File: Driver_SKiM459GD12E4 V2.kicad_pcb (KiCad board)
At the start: 4 copper layers, 169.2 x 116 mm, 97 parts, among them J13 EL1, J14 GL1, J15 NTC1_A, J16 NTC1_B, J17 GH1, J18 OUT1, J19 CH1, J20 EL2, J21 GL2, J22 NTC2_A, J23 NTC2_B, J24 GH2, J25 OUT2, J26 CH2, J27 EL3, J28 GL3, J29 NTC3_A, J30 NTC3_B, J31 GH3, J32 OUT3, J33 CH3

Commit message: Одна стойка
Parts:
- removed the C2 at (147.4, 114.2)
- removed the C2 at (196.2, 114.2)
- removed the C3 at (207.9, 92.6)
- removed the C3 at (159.1, 92.6)
- removed the C5 at (131.7, 114.4)
- removed the C5 at (180.5, 114.4)
- removed the C6 at (137.8, 92.6)
- removed the C6 at (186.6, 92.6)
- removed the D1 at (148.5, 105.8)
- removed the D1 at (197.2, 105.8)
- removed the D2 at (154.1, 74.3)
- removed the D2 at (202.8, 74.3)
- removed the D3 at (205.4, 92.1)
- removed the D3 at (156.6, 92.1)
- removed the D4 at (132.2, 105.8)
- removed the D4 at (181.0, 105.8)
- removed the D5 at (183.8, 92.1)
- removed the D5 at (135.0, 92.1)
- removed the D6 at (132.3, 74.3)
- removed the D6 at (181.1, 74.3)
- removed the R1 at (198.5, 114.2)
- removed the R1 at (149.7, 114.2)
- removed the R10 at (181.1, 92.6)
- removed the R10 at (132.3, 92.6)
- removed the R12 at (132.3, 82.9)
- removed the R12 at (181.1, 82.9)
- removed the R2 at (145.4, 90.6)
- removed the R2 at (194.2, 90.6)
- removed the R3 at (199.0, 90.6)
- removed the R3 at (150.2, 90.6)
- removed the R4 at (202.8, 82.9)
- removed the R4 at (154.1, 82.9)
- removed the R5 at (154.1, 92.6)
- removed the R5 at (202.8, 92.6)
- removed the R7 at (182.8, 114.4)
- removed the R7 at (134.0, 114.4)
- removed the R8 at (172.4, 90.8)
- removed the R8 at (123.7, 90.8)
- removed the R9 at (128.5, 90.8)
- removed the R9 at (177.3, 90.8)
- added C10: 2.2u, Capacitor_SMD:C_0805_2012Metric_Pad1.18x1.45mm_HandSolder, B.Cu at (97.8, 118.9)
- added C11: 56p, Capacitor_SMD:C_0805_2012Metric_Pad1.18x1.45mm_HandSolder, F.Cu at (74.2, 137.4)
- added C12: 56p, Capacitor_SMD:C_0805_2012Metric_Pad1.18x1.45mm_HandSolder, B.Cu at (67.3, 133.1)
- added C13: 56p, Capacitor_SMD:C_0805_2012Metric_Pad1.18x1.45mm_HandSolder, B.Cu at (90.2, 125.5)
- added C14: 56p, Capacitor_SMD:C_0805_2012Metric_Pad1.18x1.45mm_HandSolder, B.Cu at (86.6, 141.7)
- added C15: 56p, Capacitor_SMD:C_0805_2012Metric_Pad1.18x1.45mm_HandSolder, F.Cu at (92.7, 130.3)
- added C16: 56p, Capacitor_SMD:C_0805_2012Metric_Pad1.18x1.45mm_HandSolder, F.Cu at (92.7, 144.0)
- added C17: 56p, Capacitor_SMD:C_0805_2012Metric_Pad1.18x1.45mm_HandSolder, F.Cu at (92.7, 134.9)
- added C18: 56p, Capacitor_SMD:C_0805_2012Metric_Pad1.18x1.45mm_HandSolder, F.Cu at (92.7, 139.4)
- added C19: 10u, Capacitor_SMD:C_1210_3225Metric_Pad1.33x2.70mm_HandSolder, F.Cu at (82.3, 118.9)
- added C20: 10u, Capacitor_SMD:C_1210_3225Metric_Pad1.33x2.70mm_HandSolder, F.Cu at (93.0, 118.9)
- added C21: 1u, Capacitor_SMD:C_0805_2012Metric_Pad1.18x1.45mm_HandSolder, B.Cu at (102.6, 99.6)
- added C22: 1u, Capacitor_SMD:C_0805_2012Metric_Pad1.18x1.45mm_HandSolder, B.Cu at (99.8, 99.6)
- added C23: 10u, Capacitor_SMD:C_1210_3225Metric_Pad1.33x2.70mm_HandSolder, F.Cu at (79.8, 92.7)
- added C24: 10u, Capacitor_SMD:C_1210_3225Metric_Pad1.33x2.70mm_HandSolder, F.Cu at (85.1, 92.7)
- added C25: 10u, Capacitor_SMD:C_1210_3225Metric_Pad1.33x2.70mm_HandSolder, F.Cu at (90.7, 92.7)
- added C26: 10u, Capacitor_SMD:C_1210_3225Metric_Pad1.33x2.70mm_HandSolder, F.Cu at (96.1, 92.7)
- added C27: 1u, Capacitor_SMD:C_0805_2012Metric_Pad1.18x1.45mm_HandSolder, B.Cu at (68.6, 100.6)
- added C28: 1u, Capacitor_SMD:C_0805_2012Metric_Pad1.18x1.45mm_HandSolder, B.Cu at (65.8, 100.6)
- added C7: 56p, Capacitor_SMD:C_0805_2012Metric_Pad1.18x1.45mm_HandSolder, F.Cu at (103.4, 124.2)
- added C8: 56p, Capacitor_SMD:C_0805_2012Metric_Pad1.18x1.45mm_HandSolder, F.Cu at (68.6, 124.2)
- added C9: 2.2u, Capacitor_SMD:C_0805_2012Metric_Pad1.18x1.45mm_HandSolder, B.Cu at (63.0, 118.9)
- added D10: FLT, LED_SMD:LED_0805_2012Metric_Pad1.15x1.40mm_HandSolder, F.Cu at (73.9, 122.7)
- added D11: RDY, LED_SMD:LED_0805_2012Metric_Pad1.15x1.40mm_HandSolder, F.Cu at (73.9, 125.0)
- added D12: FLT, LED_SMD:LED_0805_2012Metric_Pad1.15x1.40mm_HandSolder, F.Cu at (109.0, 122.7)
- added D13: RDY, LED_SMD:LED_0805_2012Metric_Pad1.15x1.40mm_HandSolder, F.Cu at (109.0, 125.0)
- added D14: SN74AC08DR, Package_SO:SOIC-14_3.9x8.7mm_P1.27mm, F.Cu at (100.0, 136.4)
- added D15: WRA1215S-3WR2, Mornsun:WRA1215S-3WR2, F.Cu at (80.1, 105.7)
- added D16: WRA1215S-3WR2, Mornsun:WRA1215S-3WR2, F.Cu at (90.8, 105.7)
- added D7: SN74AHC1G32DBVR, Package_TO_SOT_SMD:SOT-23-5_HandSoldering, B.Cu at (85.3, 130.8)
- added D8: SN74AHC1G86DBVR, Package_TO_SOT_SMD:SOT-23-5_HandSoldering, F.Cu at (100.8, 118.9)
- added D9: SN74AHC1G86DBVR, Package_TO_SOT_SMD:SOT-23-5_HandSoldering, F.Cu at (66.0, 119.0)
- added Q1: MJD44H11T4G, Package_TO_SOT_SMD:TO-252-2, F.Cu at (98.8, 61.3)
- added Q2: MJD45H11T4G, Package_TO_SOT_SMD:TO-252-2, F.Cu at (91.2, 61.3)
- added Q3: MJD44H11T4G, Package_TO_SOT_SMD:TO-252-2, F.Cu at (70.1, 61.2)
- added Q4: MJD45H11T4G, Package_TO_SOT_SMD:TO-252-2, F.Cu at (78.2, 61.2)
- added R13: 10k, Resistor_SMD:R_0805_2012Metric_Pad1.20x1.40mm_HandSolder, B.Cu at (82.5, 137.9)
- added R14: 10k, Resistor_SMD:R_0805_2012Metric_Pad1.20x1.40mm_HandSolder, B.Cu at (82.5, 135.6)
- added R15: 120, Resistor_SMD:R_0805_2012Metric_Pad1.20x1.40mm_HandSolder, F.Cu at (100.8, 124.2)
- added R16: 120, Resistor_SMD:R_0805_2012Metric_Pad1.20x1.40mm_HandSolder, F.Cu at (66.0, 124.2)
- added R17: 330, Resistor_SMD:R_0805_2012Metric_Pad1.20x1.40mm_HandSolder, B.Cu at (77.7, 122.7)
- added R18: 330, Resistor_SMD:R_0805_2012Metric_Pad1.20x1.40mm_HandSolder, B.Cu at (73.9, 126.5)
- added R19: 10k, Resistor_SMD:R_0805_2012Metric_Pad1.20x1.40mm_HandSolder, F.Cu at (74.2, 140.0)
- added R20: 120, Resistor_SMD:R_0805_2012Metric_Pad1.20x1.40mm_HandSolder, B.Cu at (67.3, 135.6)
- added R21: 10k, Resistor_SMD:R_0805_2012Metric_Pad1.20x1.40mm_HandSolder, B.Cu at (92.7, 125.5)
- added R22: 330, Resistor_SMD:R_0805_2012Metric_Pad1.20x1.40mm_HandSolder, B.Cu at (114.0, 122.7)
- added R23: 330, Resistor_SMD:R_0805_2012Metric_Pad1.20x1.40mm_HandSolder, B.Cu at (109.0, 125.0)
- added R24: 120, Resistor_SMD:R_0805_2012Metric_Pad1.20x1.40mm_HandSolder, B.Cu at (86.6, 144.3)
- added R25: 120, Resistor_SMD:R_0805_2012Metric_Pad1.20x1.40mm_HandSolder, F.Cu at (92.7, 128.0)
- added R26: 120, Resistor_SMD:R_0805_2012Metric_Pad1.20x1.40mm_HandSolder, F.Cu at (92.7, 132.6)
- added R27: 120, Resistor_SMD:R_0805_2012Metric_Pad1.20x1.40mm_HandSolder, F.Cu at (92.7, 137.2)
- added R28: 120, Resistor_SMD:R_0805_2012Metric_Pad1.20x1.40mm_HandSolder, F.Cu at (92.7, 141.7)
- added R29: 3.9, Resistor_SMD:R_2512_6332Metric_Pad1.40x3.35mm_HandSolder, F.Cu at (99.8, 72.4)
- added R30: 3.9, Resistor_SMD:R_2512_6332Metric_Pad1.40x3.35mm_HandSolder, F.Cu at (78.0, 72.4)
- D2, D6: moved to B.Cu
- R11, R6: moved to F.Cu
- moved C4 26.8 mm to (109.0, 115.6), turned to 180 degrees
- moved C1 23.8 mm to (73.9, 115.6), turned to 180 degrees
- moved R9 19.4 mm to (72.1, 72.4)
- moved R8 19.3 mm to (67.8, 72.4)
- moved R2 19.2 mm to (88.9, 72.4)
- moved R3 19.2 mm to (93.7, 72.4)
- moved R6 19.1 mm to (109.2, 98.3), turned to 0 degrees
- moved D6 16.0 mm to (97.5, 75.7), turned to 180 degrees
- moved C6 15.6 mm to (73.2, 99.6), turned to 180 degrees
- moved C2 13.5 mm to (109.0, 120.1), turned to 180 degrees
- moved D5 11.9 mm to (72.4, 91.9), turned to -90 degrees
- moved D4 11.7 mm to (70.2, 108.8)
- moved R10 11.1 mm to (72.4, 86.6)
- moved R1 10.5 mm to (109.0, 117.9), turned to 180 degrees
- moved R7 9.93 mm to (73.9, 117.8), turned to 180 degrees
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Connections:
- net -8V_H1 renamed -15V_H1
- net -8V_L1 renamed -15V_L1
- D1 pad 15: GH1 -> unconnected-(D1-Pad15)
- D4 pad 15: GL1 -> unconnected-(D4-Pad15)
- R2 pad 1: GH1 -> BH1_CLOSE
- R3 pad 1: GH1 -> BH1_CLOSE
- R8 pad 1: GL1 -> BL1_CLOSE
- R9 pad 1: GL1 -> BL1_CLOSE
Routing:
- net OUT1: track 6.28 -> 82.6 mm
- net GL1: track 81.3 -> 14.4 mm, vias 3 -> 1
- net FLT_L1: track 0.00 -> 55.8 mm, vias 0 -> 3
- net GH1: track 69.6 -> 15.4 mm, vias 3 -> 1
- net RDY_L1: track 0.00 -> 53.3 mm, vias 0 -> 2
- net Net-(D7-Pad4): track 0.00 -> 52.8 mm, vias 0 -> 2
- net RDY_H1: track 0.00 -> 49.3 mm, vias 0 -> 2
- net EL1: track 0.00 -> 45.6 mm, vias 0 -> 2
- net FLT_H1: track 0.00 -> 34.7 mm, vias 0 -> 2
- net GND3: track 26.2 -> 59.4 mm, vias 9 -> 26
- net PWM_Input_H1: track 0.00 -> 32.3 mm, vias 0 -> 1
- net PWM_Input_L1: track 0.00 -> 31.7 mm, vias 0 -> 3
- net Net-(C6-Pad1): track 39.5 -> 17.9 mm
- net Net-(C3-Pad1): track 40.2 -> 19.8 mm
- net Net-(R10-Pad1): track 21.3 -> 2.28 mm
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- added copper zone on In1.Cu, net +15V_H1
- added copper zone on In1.Cu, net +15V_L1
- added copper zone on In1.Cu, net +5VD
- added copper zone on In2.Cu, net -15V_H1
- added copper zone on In2.Cu, net -15V_L1
- added copper zone on In2.Cu, net GND3
- added copper zone on B.Cu, net Net-(Q3-Pad3)
- removed copper zone on B.Cu, net CH1
- removed copper zone on B.Cu, net GH1
- removed copper zone on B.Cu, net GL1
- removed copper zone on B.Cu, net OUT1

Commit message: Первая сырая расстановка, неполная
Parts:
- added C29: 0.1u, Capacitor_SMD:C_0805_2012Metric_Pad1.18x1.45mm_HandSolder, B.Cu at (174.0, 116.1)
- added C30: 0.1u, Capacitor_SMD:C_0805_2012Metric_Pad1.18x1.45mm_HandSolder, B.Cu at (124.0, 115.6)
- added C31: 56p, Capacitor_SMD:C_0805_2012Metric_Pad1.18x1.45mm_HandSolder, F.Cu at (124.0, 120.1)
- added C32: 56p, Capacitor_SMD:C_0805_2012Metric_Pad1.18x1.45mm_HandSolder, F.Cu at (158.8, 120.1)
- added C33: 220p, Capacitor_SMD:C_0805_2012Metric_Pad1.18x1.45mm_HandSolder, F.Cu at (159.0, 96.0)
- added C34: 220p, Capacitor_SMD:C_0805_2012Metric_Pad1.18x1.45mm_HandSolder, F.Cu at (123.2, 99.6)
- added C35: 1u, Capacitor_SMD:C_0805_2012Metric_Pad1.18x1.45mm_HandSolder, B.Cu at (152.4, 99.6)
- added C36: 1u, Capacitor_SMD:C_0805_2012Metric_Pad1.18x1.45mm_HandSolder, B.Cu at (149.6, 99.6)
- added C37: 1u, Capacitor_SMD:C_0805_2012Metric_Pad1.18x1.45mm_HandSolder, B.Cu at (118.4, 100.6)
- added C38: 1u, Capacitor_SMD:C_0805_2012Metric_Pad1.18x1.45mm_HandSolder, B.Cu at (115.6, 100.6)
- added C39: 0.1u, Capacitor_SMD:C_0805_2012Metric_Pad1.18x1.45mm_HandSolder, B.Cu at (209.0, 116.1)
- added C40: 0.1u, Capacitor_SMD:C_0805_2012Metric_Pad1.18x1.45mm_HandSolder, B.Cu at (158.8, 116.1)
- added C41: 56p, Capacitor_SMD:C_0805_2012Metric_Pad1.18x1.45mm_HandSolder, F.Cu at (174.0, 120.1)
- added C42: 56p, Capacitor_SMD:C_0805_2012Metric_Pad1.18x1.45mm_HandSolder, F.Cu at (209.0, 120.1)
- added C43: 220p, Capacitor_SMD:C_0805_2012Metric_Pad1.18x1.45mm_HandSolder, F.Cu at (209.6, 96.0)
- added C44: 220p, Capacitor_SMD:C_0805_2012Metric_Pad1.18x1.45mm_HandSolder, F.Cu at (173.2, 99.6)
- added C45: 1u, Capacitor_SMD:C_0805_2012Metric_Pad1.18x1.45mm_HandSolder, B.Cu at (202.7, 99.6)
- added C46: 1u, Capacitor_SMD:C_0805_2012Metric_Pad1.18x1.45mm_HandSolder, B.Cu at (199.9, 99.6)
- added C47: 1u, Capacitor_SMD:C_0805_2012Metric_Pad1.18x1.45mm_HandSolder, B.Cu at (168.4, 100.3)
- added C48: 1u, Capacitor_SMD:C_0805_2012Metric_Pad1.18x1.45mm_HandSolder, B.Cu at (165.6, 100.3)
- added C49: 10u, Capacitor_SMD:C_1210_3225Metric_Pad1.33x2.70mm_HandSolder, F.Cu at (132.3, 118.9)
- added C50: 10u, Capacitor_SMD:C_1210_3225Metric_Pad1.33x2.70mm_HandSolder, F.Cu at (142.7, 118.9)
- added C51: 10u, Capacitor_SMD:C_1210_3225Metric_Pad1.33x2.70mm_HandSolder, F.Cu at (129.8, 92.7)
- added C52: 10u, Capacitor_SMD:C_1210_3225Metric_Pad1.33x2.70mm_HandSolder, F.Cu at (135.1, 92.7)
- added C53: 10u, Capacitor_SMD:C_1210_3225Metric_Pad1.33x2.70mm_HandSolder, F.Cu at (140.7, 92.7)
- added C54: 10u, Capacitor_SMD:C_1210_3225Metric_Pad1.33x2.70mm_HandSolder, F.Cu at (146.0, 92.7)
- added C55: 10u, Capacitor_SMD:C_1210_3225Metric_Pad1.33x2.70mm_HandSolder, F.Cu at (193.0, 118.9)
- added C56: 10u, Capacitor_SMD:C_1210_3225Metric_Pad1.33x2.70mm_HandSolder, F.Cu at (182.4, 118.9)
- added C57: 10u, Capacitor_SMD:C_1210_3225Metric_Pad1.33x2.70mm_HandSolder, F.Cu at (190.8, 92.7)
- added C58: 10u, Capacitor_SMD:C_1210_3225Metric_Pad1.33x2.70mm_HandSolder, F.Cu at (196.1, 92.7)
- added C59: 10u, Capacitor_SMD:C_1210_3225Metric_Pad1.33x2.70mm_HandSolder, F.Cu at (179.8, 92.7)
- added C60: 10u, Capacitor_SMD:C_1210_3225Metric_Pad1.33x2.70mm_HandSolder, F.Cu at (185.2, 92.7)
- added C61: 56p, Capacitor_SMD:C_0805_2012Metric_Pad1.18x1.45mm_HandSolder, F.Cu at (126.5, 137.2)
- added C62: 56p, Capacitor_SMD:C_0805_2012Metric_Pad1.18x1.45mm_HandSolder, B.Cu at (121.2, 133.1)
- added C63: 56p, Capacitor_SMD:C_0805_2012Metric_Pad1.18x1.45mm_HandSolder, B.Cu at (140.0, 125.5)
- added C64: 56p, Capacitor_SMD:C_0805_2012Metric_Pad1.18x1.45mm_HandSolder, B.Cu at (136.9, 141.7)
- added C65: 56p, Capacitor_SMD:C_0805_2012Metric_Pad1.18x1.45mm_HandSolder, F.Cu at (142.5, 130.3)
- added C66: 56p, Capacitor_SMD:C_0805_2012Metric_Pad1.18x1.45mm_HandSolder, F.Cu at (142.5, 144.0)
- added C67: 56p, Capacitor_SMD:C_0805_2012Metric_Pad1.18x1.45mm_HandSolder, F.Cu at (142.5, 134.9)
- added C68: 56p, Capacitor_SMD:C_0805_2012Metric_Pad1.18x1.45mm_HandSolder, F.Cu at (142.5, 139.4)
- added C69: 56p, Capacitor_SMD:C_0805_2012Metric_Pad1.18x1.45mm_HandSolder, F.Cu at (173.7, 137.4)
- added C70: 56p, Capacitor_SMD:C_0805_2012Metric_Pad1.18x1.45mm_HandSolder, B.Cu at (170.9, 133.1)
- added C71: 56p, Capacitor_SMD:C_0805_2012Metric_Pad1.18x1.45mm_HandSolder, B.Cu at (190.0, 125.5)
- added C72: 56p, Capacitor_SMD:C_0805_2012Metric_Pad1.18x1.45mm_HandSolder, B.Cu at (186.9, 141.7)
- added C73: 56p, Capacitor_SMD:C_0805_2012Metric_Pad1.18x1.45mm_HandSolder, F.Cu at (192.8, 130.3)
- added C74: 56p, Capacitor_SMD:C_0805_2012Metric_Pad1.18x1.45mm_HandSolder, F.Cu at (192.8, 144.0)
- added C75: 56p, Capacitor_SMD:C_0805_2012Metric_Pad1.18x1.45mm_HandSolder, F.Cu at (192.8, 134.9)
- added C76: 56p, Capacitor_SMD:C_0805_2012Metric_Pad1.18x1.45mm_HandSolder, F.Cu at (192.8, 139.4)
- added C77: 56p, Capacitor_SMD:C_0805_2012Metric_Pad1.18x1.45mm_HandSolder, F.Cu at (153.2, 124.2)
- added C78: 56p, Capacitor_SMD:C_0805_2012Metric_Pad1.18x1.45mm_HandSolder, F.Cu at (118.6, 124.2)
- added C79: 2.2u, Capacitor_SMD:C_0805_2012Metric_Pad1.18x1.45mm_HandSolder, B.Cu at (113.0, 118.9)
- added C80: 2.2u, Capacitor_SMD:C_0805_2012Metric_Pad1.18x1.45mm_HandSolder, B.Cu at (147.6, 118.9)
- added C81: 56p, Capacitor_SMD:C_0805_2012Metric_Pad1.18x1.45mm_HandSolder, F.Cu at (203.5, 124.2)
- added C82: 56p, Capacitor_SMD:C_0805_2012Metric_Pad1.18x1.45mm_HandSolder, F.Cu at (168.4, 124.2)
- added C83: 2.2u, Capacitor_SMD:C_0805_2012Metric_Pad1.18x1.45mm_HandSolder, B.Cu at (197.9, 118.9)
- added C84: 2.2u, Capacitor_SMD:C_0805_2012Metric_Pad1.18x1.45mm_HandSolder, B.Cu at (163.3, 118.9)
- added C85: C, Capacitor_SMD:C_1206_3216Metric_Pad1.33x1.80mm_HandSolder, F.Cu at (194.6, 41.4)
- added C86: C_Small, Capacitor_SMD:C_0805_2012Metric_Pad1.18x1.45mm_HandSolder, B.Cu at (194.6, 40.9)
- added C87: C_Small, Capacitor_SMD:C_0805_2012Metric_Pad1.18x1.45mm_HandSolder, F.Cu at (196.8, 44.2)
- added C88: C_Small, Capacitor_SMD:C_0805_2012Metric_Pad1.18x1.45mm_HandSolder, F.Cu at (192.3, 44.2)
- added C89: C_Small, Capacitor_SMD:C_0805_2012Metric_Pad1.18x1.45mm_HandSolder, F.Cu at (188.2, 50.5)
- added C90: C_Small, Capacitor_SMD:C_0805_2012Metric_Pad1.18x1.45mm_HandSolder, F.Cu at (200.9, 50.5)
- added C91: 10u, Capacitor_SMD:C_1210_3225Metric_Pad1.33x2.70mm_HandSolder, F.Cu at (224.8, 114.3)
- added C92: 10u, Capacitor_SMD:C_1210_3225Metric_Pad1.33x2.70mm_HandSolder, F.Cu at (218.7, 114.3)
- added C93: 100n, Capacitor_SMD:C_0805_2012Metric_Pad1.18x1.45mm_HandSolder, F.Cu at (254.8, 132.1)
- added C94: 100n, Capacitor_SMD:C_0805_2012Metric_Pad1.18x1.45mm_HandSolder, F.Cu at (254.8, 129.1)
- added C95: 100n, Capacitor_SMD:C_0805_2012Metric_Pad1.18x1.45mm_HandSolder, F.Cu at (246.3, 139.3)
- added D17: ADUM4135, Package_SO:SOIC-16W_7.5x10.3mm_P1.27mm, F.Cu at (120.1, 108.7)
- added D18: ADUM4135, Package_SO:SOIC-16W_7.5x10.3mm_P1.27mm, F.Cu at (154.9, 108.7)
- added D19: BZT52C10-7-F, Diode_SMD:D_SOD-123, F.Cu at (158.0, 91.9)
- added D20: BZT52C10-7-F, Diode_SMD:D_SOD-123, F.Cu at (122.4, 91.9)
- added D21: US3M-13, Diode_SMD:D_SMC, B.Cu at (151.1, 66.8)
- added D22: US3M-13, Diode_SMD:D_SMC, B.Cu at (146.8, 75.7)
- added D23: ADUM4135, Package_SO:SOIC-16W_7.5x10.3mm_P1.27mm, F.Cu at (170.2, 108.7)
- added D24: ADUM4135, Package_SO:SOIC-16W_7.5x10.3mm_P1.27mm, F.Cu at (205.2, 108.7)
- added D25: BZT52C10-7-F, Diode_SMD:D_SOD-123, F.Cu at (208.5, 91.9)
- added D26: BZT52C10-7-F, Diode_SMD:D_SOD-123, F.Cu at (172.2, 91.9)
- added D27: US3M-13, Diode_SMD:D_SMC, B.Cu at (200.9, 66.8)
- added D28: US3M-13, Diode_SMD:D_SMC, B.Cu at (196.6, 75.7)
- added D29: WRA1215S-3WR2, Mornsun:WRA1215S-3WR2, F.Cu at (130.0, 105.7)
- added D30: WRA1215S-3WR2, Mornsun:WRA1215S-3WR2, F.Cu at (140.7, 105.7)
- added D31: WRA1215S-3WR2, Mornsun:WRA1215S-3WR2, F.Cu at (190.8, 105.7)
- added D32: WRA1215S-3WR2, Mornsun:WRA1215S-3WR2, F.Cu at (180.2, 105.7)
- added D33: FLT, LED_SMD:LED_0805_2012Metric_Pad1.15x1.40mm_HandSolder, F.Cu at (124.0, 122.7)
- added D34: RDY, LED_SMD:LED_0805_2012Metric_Pad1.15x1.40mm_HandSolder, F.Cu at (124.0, 125.0)
- added D35: FLT, LED_SMD:LED_0805_2012Metric_Pad1.15x1.40mm_HandSolder, F.Cu at (158.8, 122.7)
- added D36: RDY, LED_SMD:LED_0805_2012Metric_Pad1.15x1.40mm_HandSolder, F.Cu at (158.8, 125.0)
- added D37: SN74AC08DR, Package_SO:SOIC-14_3.9x8.7mm_P1.27mm, F.Cu at (149.9, 136.4)
- added D38: FLT, LED_SMD:LED_0805_2012Metric_Pad1.15x1.40mm_HandSolder, F.Cu at (174.0, 122.7)
- added D39: RDY, LED_SMD:LED_0805_2012Metric_Pad1.15x1.40mm_HandSolder, F.Cu at (174.0, 125.0)
- added D40: FLT, LED_SMD:LED_0805_2012Metric_Pad1.15x1.40mm_HandSolder, F.Cu at (209.0, 122.7)
- added D41: RDY, LED_SMD:LED_0805_2012Metric_Pad1.15x1.40mm_HandSolder, F.Cu at (209.0, 125.0)
- added D42: SN74AC08DR, Package_SO:SOIC-14_3.9x8.7mm_P1.27mm, F.Cu at (200.7, 136.4)
- added D43: SN74AHC1G32DBVR, Package_TO_SOT_SMD:SOT-23-5_HandSoldering, B.Cu at (133.3, 130.6)
- added D44: SN74AHC1G86DBVR, Package_TO_SOT_SMD:SOT-23-5_HandSoldering, F.Cu at (150.6, 118.9)
- added D45: SN74AHC1G86DBVR, Package_TO_SOT_SMD:SOT-23-5_HandSoldering, F.Cu at (116.1, 118.9)
- added D46: SN74AHC1G32DBVR, Package_TO_SOT_SMD:SOT-23-5_HandSoldering, B.Cu at (183.9, 130.6)
- added D47: SN74AHC1G86DBVR, Package_TO_SOT_SMD:SOT-23-5_HandSoldering, F.Cu at (200.9, 118.9)
- added D48: SN74AHC1G86DBVR, Package_TO_SOT_SMD:SOT-23-5_HandSoldering, F.Cu at (165.9, 118.9)
- added D49: D_Zener_Small, Diode_SMD:D_SMB, F.Cu at (179.6, 50.3)
- added D50: D_Zener_Small, Diode_SMD:D_SMB, F.Cu at (209.8, 50.5)
- added D51: SN74HC11DR, Package_SO:SOIC-14_3.9x8.7mm_P1.27mm, F.Cu at (248.1, 132.7)
- added D52: CD4504B, Package_SO:SOP-16_3.9x9.9mm_P1.27mm, F.Cu at (239.6, 133.3)
- added J1: 2-338069-0, Connector_My:2-338069-0, F.Cu at (226.8, 146.2)
- added Q10: MJD45H11T4G, Package_TO_SOT_SMD:TO-252-2, F.Cu at (191.5, 61.2)
- added Q11: MJD44H11T4G, Package_TO_SOT_SMD:TO-252-2, F.Cu at (170.4, 61.2)
- added Q12: MJD45H11T4G, Package_TO_SOT_SMD:TO-252-2, F.Cu at (178.6, 61.2)
- added Q5: MJD44H11T4G, Package_TO_SOT_SMD:TO-252-2, F.Cu at (148.8, 61.2)
- added Q6: MJD45H11T4G, Package_TO_SOT_SMD:TO-252-2, F.Cu at (141.2, 61.2)
- added Q7: MJD44H11T4G, Package_TO_SOT_SMD:TO-252-2, F.Cu at (120.1, 61.4)
- added Q8: MJD45H11T4G, Package_TO_SOT_SMD:TO-252-2, F.Cu at (128.3, 61.4)
- added Q9: MJD44H11T4G, Package_TO_SOT_SMD:TO-252-2, F.Cu at (199.1, 61.2)
- added R100: 910k, Resistor_SMD:R_0805_2012Metric_Pad1.20x1.40mm_HandSolder, B.Cu at (214.6, 51.1)
- added R101: 910k, Resistor_SMD:R_0805_2012Metric_Pad1.20x1.40mm_HandSolder, B.Cu at (164.6, 70.1)
- added R102: 910k, Resistor_SMD:R_0805_2012Metric_Pad1.20x1.40mm_HandSolder, B.Cu at (164.6, 74.7)
- added R103: 910k, Resistor_SMD:R_0805_2012Metric_Pad1.20x1.40mm_HandSolder, B.Cu at (164.6, 79.2)
- added R104: 910k, Resistor_SMD:R_0805_2012Metric_Pad1.20x1.40mm_HandSolder, B.Cu at (164.6, 83.8)
- added R105: 910k, Resistor_SMD:R_0805_2012Metric_Pad1.20x1.40mm_HandSolder, B.Cu at (210.3, 51.1)
- added R106: 910k, Resistor_SMD:R_0805_2012Metric_Pad1.20x1.40mm_HandSolder, B.Cu at (164.6, 65.5)
- added R107: 910k, Resistor_SMD:R_0805_2012Metric_Pad1.20x1.40mm_HandSolder, B.Cu at (206.0, 51.1)
- added R108: 910k, Resistor_SMD:R_0805_2012Metric_Pad1.20x1.40mm_HandSolder, B.Cu at (164.6, 61.0)
- added R109: 910k, Resistor_SMD:R_0805_2012Metric_Pad1.20x1.40mm_HandSolder, B.Cu at (201.7, 51.1)
- added R110: 910k, Resistor_SMD:R_0805_2012Metric_Pad1.20x1.40mm_HandSolder, B.Cu at (162.8, 57.1)
- added R111: 910k, Resistor_SMD:R_0805_2012Metric_Pad1.20x1.40mm_HandSolder, B.Cu at (199.9, 47.8)
- added R112: 910k, Resistor_SMD:R_0805_2012Metric_Pad1.20x1.40mm_HandSolder, B.Cu at (159.8, 53.6)
- added R113: 3k, Resistor_SMD:R_0805_2012Metric_Pad1.20x1.40mm_HandSolder, B.Cu at (190.2, 40.9)
- added R114: 3.3k, Resistor_SMD:R_0805_2012Metric_Pad1.20x1.40mm_HandSolder, B.Cu at (198.9, 40.9)
- added R115: 910k, Resistor_SMD:R_0805_2012Metric_Pad1.20x1.40mm_HandSolder, B.Cu at (203.2, 46.0)
- added R116: 910k, Resistor_SMD:R_0805_2012Metric_Pad1.20x1.40mm_HandSolder, B.Cu at (159.8, 49.0)
- added R117: 910k, Resistor_SMD:R_0805_2012Metric_Pad1.20x1.40mm_HandSolder, B.Cu at (206.5, 44.5)
- added R118: 27k, Resistor_SMD:R_0805_2012Metric_Pad1.20x1.40mm_HandSolder, F.Cu at (198.9, 40.9)
- added R119: 27k, Resistor_SMD:R_0805_2012Metric_Pad1.20x1.40mm_HandSolder, F.Cu at (190.2, 40.9)
- added R120: 910k, Resistor_SMD:R_0805_2012Metric_Pad1.20x1.40mm_HandSolder, B.Cu at (162.8, 45.2)
- added R121: 1k, Resistor_SMD:R_0805_2012Metric_Pad1.20x1.40mm_HandSolder, F.Cu at (186.9, 47.0)
- added R122: 1k, Resistor_SMD:R_0805_2012Metric_Pad1.20x1.40mm_HandSolder, F.Cu at (202.2, 47.0)
- added R123: 10, Resistor_SMD:R_0805_2012Metric_Pad1.20x1.40mm_HandSolder, F.Cu at (185.7, 50.5)
- added R124: 10, Resistor_SMD:R_0805_2012Metric_Pad1.20x1.40mm_HandSolder, F.Cu at (203.7, 50.5)
- added R125: 2k, Resistor_SMD:R_0805_2012Metric_Pad1.20x1.40mm_HandSolder, F.Cu at (100.8, 128.5)
- added R126: 1k, Resistor_SMD:R_0805_2012Metric_Pad1.20x1.40mm_HandSolder, F.Cu at (98.3, 128.5)
- added R127: 2k, Resistor_SMD:R_0805_2012Metric_Pad1.20x1.40mm_HandSolder, B.Cu at (62.0, 126.2)
- added R128: 1k, Resistor_SMD:R_0805_2012Metric_Pad1.20x1.40mm_HandSolder, B.Cu at (64.5, 126.2)
- added R129: 2k, Resistor_SMD:R_0805_2012Metric_Pad1.20x1.40mm_HandSolder, F.Cu at (150.6, 128.3)
- added R130: 1k, Resistor_SMD:R_0805_2012Metric_Pad1.20x1.40mm_HandSolder, F.Cu at (148.3, 128.3)
- added R131: 2k, Resistor_SMD:R_0805_2012Metric_Pad1.20x1.40mm_HandSolder, B.Cu at (116.1, 128.3)
- added R132: 1k, Resistor_SMD:R_0805_2012Metric_Pad1.20x1.40mm_HandSolder, B.Cu at (113.5, 128.3)
- added R133: 2k, Resistor_SMD:R_0805_2012Metric_Pad1.20x1.40mm_HandSolder, F.Cu at (200.9, 128.3)
- added R134: 1k, Resistor_SMD:R_0805_2012Metric_Pad1.20x1.40mm_HandSolder, F.Cu at (198.6, 128.3)
- added R135: 2k, Resistor_SMD:R_0805_2012Metric_Pad1.20x1.40mm_HandSolder, B.Cu at (165.9, 128.5)
- added R136: 1k, Resistor_SMD:R_0805_2012Metric_Pad1.20x1.40mm_HandSolder, B.Cu at (163.6, 128.5)
- added R137: 10k, Resistor_SMD:R_0805_2012Metric_Pad1.20x1.40mm_HandSolder, F.Cu at (251.1, 139.2)
- added R31: 10k, Resistor_SMD:R_1210_3225Metric_Pad1.30x2.65mm_HandSolder, B.Cu at (106.9, 81.5)
- added R32: 10k, Resistor_SMD:R_1210_3225Metric_Pad1.30x2.65mm_HandSolder, B.Cu at (72.9, 93.7)
- added R33: 120, Resistor_SMD:R_0805_2012Metric_Pad1.20x1.40mm_HandSolder, F.Cu at (123.9, 117.9)
- added R34: 120, Resistor_SMD:R_0805_2012Metric_Pad1.20x1.40mm_HandSolder, F.Cu at (158.8, 117.9)
- added R35: 3.9, Resistor_SMD:R_2512_6332Metric_Pad1.40x3.35mm_HandSolder, F.Cu at (117.9, 72.4)
- added R36: 3.9, Resistor_SMD:R_2512_6332Metric_Pad1.40x3.35mm_HandSolder, F.Cu at (122.7, 72.4)
- added R37: 3.9, Resistor_SMD:R_2512_6332Metric_Pad1.40x3.35mm_HandSolder, F.Cu at (138.9, 72.4)
- added R38: 3.9, Resistor_SMD:R_2512_6332Metric_Pad1.40x3.35mm_HandSolder, F.Cu at (143.8, 72.4)
- added R39: 1.1k, Resistor_SMD:R_0805_2012Metric_Pad1.20x1.40mm_HandSolder, F.Cu at (122.4, 86.6)
- added R40: 1.1k, Resistor_SMD:R_0805_2012Metric_Pad1.20x1.40mm_HandSolder, F.Cu at (158.0, 86.6)
- added R41: 0, Resistor_SMD:R_1206_3216Metric_Pad1.30x1.75mm_HandSolder, F.Cu at (158.0, 81.8)
- added R42: 2.2k, Resistor_SMD:R_0805_2012Metric_Pad1.20x1.40mm_HandSolder, F.Cu at (125.2, 96.8)
- added R43: 0, Resistor_SMD:R_1206_3216Metric_Pad1.30x1.75mm_HandSolder, F.Cu at (122.4, 81.8)
- added R44: 2.2k, Resistor_SMD:R_0805_2012Metric_Pad1.20x1.40mm_HandSolder, F.Cu at (159.0, 98.3)
- added R45: 3.9, Resistor_SMD:R_2512_6332Metric_Pad1.40x3.35mm_HandSolder, F.Cu at (150.1, 72.4)
- added R46: 3.9, Resistor_SMD:R_2512_6332Metric_Pad1.40x3.35mm_HandSolder, F.Cu at (128.5, 72.4)
- added R47: 10k, Resistor_SMD:R_1210_3225Metric_Pad1.30x2.65mm_HandSolder, B.Cu at (157.0, 81.5)
- added R48: 10k, Resistor_SMD:R_1210_3225Metric_Pad1.30x2.65mm_HandSolder, B.Cu at (122.9, 93.7)
- added R49: 120, Resistor_SMD:R_0805_2012Metric_Pad1.20x1.40mm_HandSolder, F.Cu at (174.0, 117.9)
- added R50: 120, Resistor_SMD:R_0805_2012Metric_Pad1.20x1.40mm_HandSolder, F.Cu at (209.0, 117.9)
- added R51: 3.9, Resistor_SMD:R_2512_6332Metric_Pad1.40x3.35mm_HandSolder, F.Cu at (168.1, 72.4)
- added R52: 3.9, Resistor_SMD:R_2512_6332Metric_Pad1.40x3.35mm_HandSolder, F.Cu at (173.0, 72.4)
- added R53: 3.9, Resistor_SMD:R_2512_6332Metric_Pad1.40x3.35mm_HandSolder, F.Cu at (189.2, 72.4)
- added R54: 3.9, Resistor_SMD:R_2512_6332Metric_Pad1.40x3.35mm_HandSolder, F.Cu at (194.1, 72.4)
- added R55: 1.1k, Resistor_SMD:R_0805_2012Metric_Pad1.20x1.40mm_HandSolder, F.Cu at (172.2, 86.6)
- added R56: 1.1k, Resistor_SMD:R_0805_2012Metric_Pad1.20x1.40mm_HandSolder, F.Cu at (208.5, 86.6)
- added R57: 0, Resistor_SMD:R_1206_3216Metric_Pad1.30x1.75mm_HandSolder, F.Cu at (208.5, 81.8)
- added R58: 2.2k, Resistor_SMD:R_0805_2012Metric_Pad1.20x1.40mm_HandSolder, F.Cu at (175.3, 96.8)
- added R59: 0, Resistor_SMD:R_1206_3216Metric_Pad1.30x1.75mm_HandSolder, F.Cu at (172.2, 81.8)
- added R60: 2.2k, Resistor_SMD:R_0805_2012Metric_Pad1.20x1.40mm_HandSolder, F.Cu at (209.6, 98.3)
- added R61: 3.9, Resistor_SMD:R_2512_6332Metric_Pad1.40x3.35mm_HandSolder, F.Cu at (200.4, 72.4)
- added R62: 3.9, Resistor_SMD:R_2512_6332Metric_Pad1.40x3.35mm_HandSolder, F.Cu at (179.8, 72.4)
- added R63: 10k, Resistor_SMD:R_1210_3225Metric_Pad1.30x2.65mm_HandSolder, B.Cu at (207.0, 81.8)
- added R64: 10k, Resistor_SMD:R_1210_3225Metric_Pad1.30x2.65mm_HandSolder, B.Cu at (173.0, 94.0)
- added R65: 330, Resistor_SMD:R_0805_2012Metric_Pad1.20x1.40mm_HandSolder, B.Cu at (127.8, 122.7)
- added R66: 330, Resistor_SMD:R_0805_2012Metric_Pad1.20x1.40mm_HandSolder, B.Cu at (124.0, 126.5)
- added R67: 10k, Resistor_SMD:R_0805_2012Metric_Pad1.20x1.40mm_HandSolder, F.Cu at (126.5, 139.7)
- added R68: 120, Resistor_SMD:R_0805_2012Metric_Pad1.20x1.40mm_HandSolder, B.Cu at (121.2, 135.6)
- added R69: 10k, Resistor_SMD:R_0805_2012Metric_Pad1.20x1.40mm_HandSolder, B.Cu at (142.5, 125.5)
- added R70: 330, Resistor_SMD:R_0805_2012Metric_Pad1.20x1.40mm_HandSolder, B.Cu at (163.1, 122.7)
- added R71: 330, Resistor_SMD:R_0805_2012Metric_Pad1.20x1.40mm_HandSolder, B.Cu at (158.8, 125.0)
- added R72: 120, Resistor_SMD:R_0805_2012Metric_Pad1.20x1.40mm_HandSolder, B.Cu at (136.9, 144.3)
- added R73: 120, Resistor_SMD:R_0805_2012Metric_Pad1.20x1.40mm_HandSolder, F.Cu at (142.5, 128.0)
- added R74: 120, Resistor_SMD:R_0805_2012Metric_Pad1.20x1.40mm_HandSolder, F.Cu at (142.5, 132.6)
- added R75: 120, Resistor_SMD:R_0805_2012Metric_Pad1.20x1.40mm_HandSolder, F.Cu at (142.5, 137.2)
- added R76: 120, Resistor_SMD:R_0805_2012Metric_Pad1.20x1.40mm_HandSolder, F.Cu at (142.5, 141.7)
- added R77: 330, Resistor_SMD:R_0805_2012Metric_Pad1.20x1.40mm_HandSolder, B.Cu at (177.8, 122.7)
- added R78: 330, Resistor_SMD:R_0805_2012Metric_Pad1.20x1.40mm_HandSolder, B.Cu at (174.0, 126.5)
- added R79: 10k, Resistor_SMD:R_0805_2012Metric_Pad1.20x1.40mm_HandSolder, F.Cu at (173.7, 140.0)
- added R80: 120, Resistor_SMD:R_0805_2012Metric_Pad1.20x1.40mm_HandSolder, B.Cu at (170.9, 135.6)
- added R81: 10k, Resistor_SMD:R_0805_2012Metric_Pad1.20x1.40mm_HandSolder, B.Cu at (192.5, 125.5)
- added R82: 330, Resistor_SMD:R_0805_2012Metric_Pad1.20x1.40mm_HandSolder, B.Cu at (213.6, 122.7)
- added R83: 330, Resistor_SMD:R_0805_2012Metric_Pad1.20x1.40mm_HandSolder, B.Cu at (209.0, 125.0)
- added R84: 120, Resistor_SMD:R_0805_2012Metric_Pad1.20x1.40mm_HandSolder, B.Cu at (186.9, 144.3)
- added R85: 120, Resistor_SMD:R_0805_2012Metric_Pad1.20x1.40mm_HandSolder, F.Cu at (192.8, 128.0)
- added R86: 120, Resistor_SMD:R_0805_2012Metric_Pad1.20x1.40mm_HandSolder, F.Cu at (192.8, 132.6)
- added R87: 120, Resistor_SMD:R_0805_2012Metric_Pad1.20x1.40mm_HandSolder, F.Cu at (192.8, 137.2)
- added R88: 120, Resistor_SMD:R_0805_2012Metric_Pad1.20x1.40mm_HandSolder, F.Cu at (192.8, 141.7)
- added R89: 10k, Resistor_SMD:R_0805_2012Metric_Pad1.20x1.40mm_HandSolder, B.Cu at (130.8, 137.9)
- added R90: 10k, Resistor_SMD:R_0805_2012Metric_Pad1.20x1.40mm_HandSolder, B.Cu at (130.8, 135.6)
- added R91: 120, Resistor_SMD:R_0805_2012Metric_Pad1.20x1.40mm_HandSolder, F.Cu at (150.6, 124.2)
- added R92: 120, Resistor_SMD:R_0805_2012Metric_Pad1.20x1.40mm_HandSolder, F.Cu at (116.1, 124.2)
- added R93: 10k, Resistor_SMD:R_0805_2012Metric_Pad1.20x1.40mm_HandSolder, B.Cu at (181.4, 137.9)
- added R94: 10k, Resistor_SMD:R_0805_2012Metric_Pad1.20x1.40mm_HandSolder, B.Cu at (181.4, 135.6)
- added R95: 120, Resistor_SMD:R_0805_2012Metric_Pad1.20x1.40mm_HandSolder, F.Cu at (200.9, 124.2)
- added R96: 120, Resistor_SMD:R_0805_2012Metric_Pad1.20x1.40mm_HandSolder, F.Cu at (165.9, 124.2)
- added R97: 910k, Resistor_SMD:R_0805_2012Metric_Pad1.20x1.40mm_HandSolder, B.Cu at (213.9, 62.5)
- added R98: 910k, Resistor_SMD:R_0805_2012Metric_Pad1.20x1.40mm_HandSolder, B.Cu at (216.4, 59.2)
- added R99: 910k, Resistor_SMD:R_0805_2012Metric_Pad1.20x1.40mm_HandSolder, B.Cu at (216.4, 54.9)
- added U1: LM2904, Package_SO:SO-8_3.9x4.9mm_P1.27mm, F.Cu at (194.6, 49.0)
- added U2: R-785.0-1.0, Converter_DCDC:Converter_DCDC_RECOM_R-78E-0.5_THT, F.Cu at (225.0, 108.4)
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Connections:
- net /Indication_ADUM/FLT renamed /Indication_ADUM_1/FLT
- net /Indication_ADUM/RDY renamed /Indication_ADUM_1/RDY
- net GND3 renamed GND
- net PWM_Input_H1 renamed Net-(D7-Pad1)
- net PWM_Input_L1 renamed Net-(D7-Pad2)
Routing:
- net GND: track 59.4 -> 268.0 mm, vias 26 -> 79
- net HB1_BOT: track 0.00 -> 179.0 mm, vias 0 -> 3
- net +15V: track 16.3 -> 165.5 mm, vias 2 -> 9
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- added copper zone on In2.Cu, net +15V
- added copper zone on In1.Cu, net +15V_H2
- added copper zone on In1.Cu, net +15V_H3
- added copper zone on In1.Cu, net +15V_L2
- added copper zone on In1.Cu, net +15V_L3
- added copper zone on In2.Cu, net -15V_H2
- added copper zone on In2.Cu, net -15V_H3
- added copper zone on In2.Cu, net -15V_L2
- added copper zone on In2.Cu, net -15V_L3
- added copper zone on B.Cu, net GND
- added copper zone on F.Cu, net GND
- added copper zone on B.Cu, net Net-(Q11-Pad3)
- added copper zone on B.Cu, net Net-(Q7-Pad3)
- added copper zone on B.Cu, net OUT1
- added copper zone on B.Cu, net OUT2
- added copper zone on B.Cu, net OUT3
- removed copper zone on In2.Cu, net GND

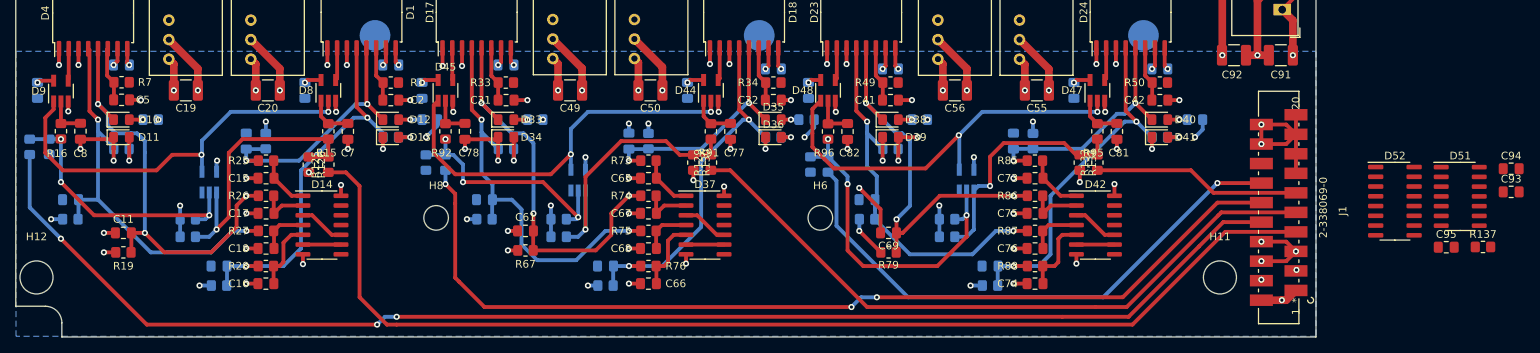
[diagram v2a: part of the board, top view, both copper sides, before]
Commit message: Всё влезло, осталься компаратор на NTC
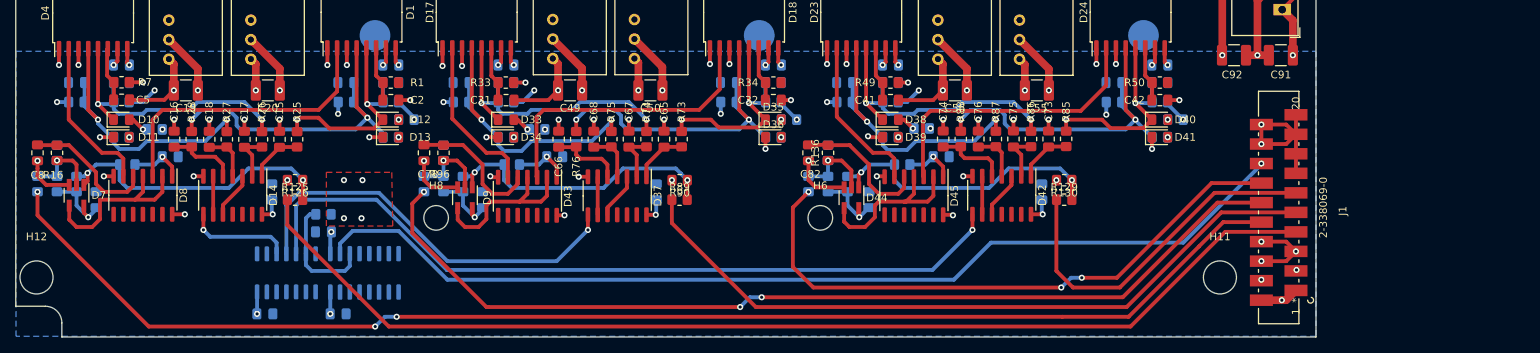
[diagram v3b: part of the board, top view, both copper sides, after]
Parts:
- removed D46: SN74AHC1G32DBVR, Package_TO_SOT_SMD:SOT-23-5_HandSoldering
- removed D47, D48: SN74AHC1G86DBVR, Package_TO_SOT_SMD:SOT-23-5_HandSoldering
- C11, C61, C69, C7, C77, C81, C93, C94, C95, D51, D52, R137, R15, R19, R67, R79, R95: moved to B.Cu
- D43: value SN74AHC1G32DBVR -> SN74AC86DR; footprint Package_TO_SOT_SMD:SOT-23-5_HandSoldering -> Package_SO:SOIC-14_3.9x8.7mm_P1.27mm; moved to F.Cu
- D44, D9: value SN74AHC1G86DBVR -> SN74AHC1G32DBVR
- D45, D8: value SN74AHC1G86DBVR -> SN74AC86DR; footprint Package_TO_SOT_SMD:SOT-23-5_HandSoldering -> Package_SO:SOIC-14_3.9x8.7mm_P1.27mm
- D7: moved to F.Cu
- R133: value 2k -> 10k; moved to B.Cu
- R134: value 1k -> 10k; moved to B.Cu
- R135: value 2k -> 120
- R136: value 1k -> 120; moved to F.Cu
- R89: value 10k -> 2k; moved to F.Cu
- R90: value 10k -> 1k; moved to F.Cu
- R91: value 120 -> 2k; moved to B.Cu
- R92: value 120 -> 1k; moved to B.Cu
- moved C94 163.3 mm to (92.6, 148.0)
- moved C93 154.6 mm to (100.2, 137.3), turned to 180 degrees
- moved D51 153.1 mm to (95.4, 142.6), turned to -90 degrees
- moved R137 150.9 mm to (100.2, 135.0), turned to 180 degrees
- moved C95 144.5 mm to (102.1, 148.0)
- moved D52 134.4 mm to (105.5, 142.6), turned to -90 degrees
- moved R95 76.3 mm to (124.7, 128.5), turned to 0 degrees
- moved R94 65.7 mm to (115.8, 131.1), turned to 90 degrees
- moved R93 63.4 mm to (118.4, 131.1), turned to 90 degrees
- moved D45 62.5 mm to (177.0, 132.6), turned to -90 degrees
- moved D9 54.4 mm to (118.6, 132.8), turned to -90 degrees
- moved R132 52.3 mm to (165.9, 127.0), turned to 90 degrees
- moved R96 50.1 mm to (115.8, 127.0)
- moved R130 48.3 mm to (196.6, 130.6), turned to 180 degrees
- moved R131 47.3 mm to (163.3, 131.1)
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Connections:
- D43 pad 1: Net-(D43-Pad1) -> Net-(C77-Pad1)
- D43 pad 3: GND -> PWM_H2
- D43 pad 4: Net-(D43-Pad4) -> Net-(D43-Pad2)
- D43 pad 5: +5VD -> Net-(C78-Pad1)
- D44 pad 1: Net-(C77-Pad1) -> Net-(D44-Pad1)
- D44 pad 2: Net-(D43-Pad4) -> Net-(D44-Pad2)
- D44 pad 4: PWM_H2 -> Net-(D44-Pad4)
- D45 pad 1: Net-(D43-Pad4) -> Net-(C81-Pad1)
- D45 pad 2: Net-(C78-Pad1) -> Net-(D44-Pad4)
- D45 pad 3: GND -> PWM_H3
- D45 pad 4: PWM_L2 -> Net-(D44-Pad4)
- D45 pad 5: +5VD -> Net-(C82-Pad1)
- D51 pad 1: FAULT_1 -> unconnected-(D51-Pad1)
- D51 pad 12: FAULT_COMM -> unconnected-(D51-Pad12)
- D51 pad 13: FAULT_3 -> unconnected-(D51-Pad13)
- D51 pad 2: FAULT_2 -> unconnected-(D51-Pad2)
- D51 pad 3: unconnected-(D51-Pad3) -> FAULT_1
- D51 pad 4: unconnected-(D51-Pad4) -> FAULT_2
- D51 pad 5: unconnected-(D51-Pad5) -> FAULT_3
- D51 pad 6: unconnected-(D51-Pad6) -> FAULT_COMM
- D8 pad 3: GND -> PWM_H1
- D8 pad 4: PWM_H1 -> Net-(D7-Pad4)
- D8 pad 5: +5VD -> Net-(C8-Pad1)
- D9 pad 1: Net-(D7-Pad4) -> Net-(D9-Pad1)
- D9 pad 2: Net-(C8-Pad1) -> Net-(D9-Pad2)
- D9 pad 4: PWM_L1 -> Net-(D43-Pad2)
- R129 pad 1: HB2_TOP -> HB3_TOP
- R129 pad 2: Net-(D43-Pad1) -> Net-(D44-Pad1)
- R130 pad 1: Net-(D43-Pad1) -> Net-(D44-Pad1)
- R131 pad 1: HB2_BOT -> HB3_BOT
- R131 pad 2: Net-(D43-Pad2) -> Net-(D44-Pad2)
- R132 pad 1: Net-(D43-Pad2) -> Net-(D44-Pad2)
- R133 pad 1: HB3_TOP -> +5VD
- R133 pad 2: Net-(D46-Pad1) -> Net-(D44-Pad1)
- R134 pad 1: Net-(D46-Pad1) -> +5VD
- R134 pad 2: GND -> Net-(D44-Pad2)
- R135 pad 1: HB3_BOT -> Net-(D44-Pad1)
- R135 pad 2: Net-(D46-Pad2) -> Net-(C81-Pad1)
- R136 pad 1: Net-(D46-Pad2) -> Net-(D44-Pad2)
- R136 pad 2: GND -> Net-(C82-Pad1)
- R89 pad 1: +5VD -> HB2_TOP
- R89 pad 2: Net-(D43-Pad1) -> Net-(D9-Pad1)
- R90 pad 1: +5VD -> Net-(D9-Pad1)
- R90 pad 2: Net-(D43-Pad2) -> GND
- R91 pad 1: Net-(D43-Pad1) -> HB2_BOT
- R91 pad 2: Net-(C77-Pad1) -> Net-(D9-Pad2)
- R92 pad 1: Net-(D43-Pad2) -> Net-(D9-Pad2)
- R92 pad 2: Net-(C78-Pad1) -> GND
- R93 pad 2: Net-(D46-Pad1) -> Net-(D9-Pad1)
- R94 pad 2: Net-(D46-Pad2) -> Net-(D9-Pad2)
- R95 pad 1: Net-(D46-Pad1) -> Net-(D9-Pad1)
- R95 pad 2: Net-(C81-Pad1) -> Net-(C77-Pad1)
- R96 pad 1: Net-(D46-Pad2) -> Net-(D9-Pad2)
- R96 pad 2: Net-(C82-Pad1) -> Net-(C78-Pad1)
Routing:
- net ERR: track 0.00 -> 130.9 mm, vias 0 -> 1
- net FAULT_3: track 0.00 -> 102.6 mm, vias 0 -> 1
- net GND: track 268.0 -> 355.6 mm, vias 79 -> 70
- net Net-(D46-Pad4): track 53.7 -> 0.00 mm, vias 2 -> 0
- net FAULT_2: track 0.00 -> 53.6 mm, vias 0 -> 1
- net Net-(D43-Pad4): track 53.0 -> 0.00 mm, vias 2 -> 0
- net Net-(D46-Pad2): track 43.5 -> 0.00 mm, vias 3 -> 0
- net Net-(D44-Pad1): track 0.00 -> 39.1 mm, vias 0 -> 2
- net Net-(D9-Pad1): track 0.00 -> 38.6 mm, vias 0 -> 2
- net Net-(D43-Pad1): track 35.9 -> 0.00 mm, vias 1 -> 0
- net PWM_H2: track 4.24 -> 38.6 mm
- net PWM_H1: track 4.24 -> 38.5 mm
- net PWM_H3: track 4.24 -> 38.1 mm
- net Net-(D46-Pad1): track 31.5 -> 0.00 mm, vias 1 -> 0
- net Net-(D7-Pad4): track 52.8 -> 23.2 mm, vias 2 -> 0
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
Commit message: Почти финальная версия
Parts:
- added C100: 0.1u, Capacitor_SMD:C_0805_2012Metric_Pad1.18x1.45mm_HandSolder, B.Cu at (154.2, 130.3)
- added C96: 0.1u, Capacitor_SMD:C_0805_2012Metric_Pad1.18x1.45mm_HandSolder, B.Cu at (132.1, 86.1)
- added C97: 0.1u, Capacitor_SMD:C_0805_2012Metric_Pad1.18x1.45mm_HandSolder, B.Cu at (137.2, 86.1)
- added C98: 0.1u, Capacitor_SMD:C_0805_2012Metric_Pad1.18x1.45mm_HandSolder, B.Cu at (138.7, 81.3)
- added C99: 0.1u, Capacitor_SMD:C_0805_2012Metric_Pad1.18x1.45mm_HandSolder, F.Cu at (154.2, 138.2)
- added R138: 120, Resistor_SMD:R_0805_2012Metric_Pad1.20x1.40mm_HandSolder, F.Cu at (132.1, 88.6)
- added R139: 120, Resistor_SMD:R_0805_2012Metric_Pad1.20x1.40mm_HandSolder, F.Cu at (132.1, 86.1)
- added R140: 1.8k, Resistor_SMD:R_0805_2012Metric_Pad1.20x1.40mm_HandSolder, F.Cu at (136.9, 86.1)
- added U3: LM397, Package_TO_SOT_SMD:SOT-23-5, F.Cu at (133.6, 81.3)
- added U4: HCPL-0611, Package_SO:SOIC-8_3.9x4.9mm_P1.27mm, F.Cu at (154.2, 132.8)
- moved R69 5.49 mm to (164.0, 122.0), turned to -90 degrees
- moved R21 5.47 mm to (114.2, 122.0), turned to -90 degrees
- moved C63 5.25 mm to (164.0, 118.0), turned to 90 degrees
- moved C13 5.24 mm to (114.2, 118.0), turned to 90 degrees
- moved R82 4.97 mm to (209.0, 127.2), turned to 180 degrees
- moved R22 4.94 mm to (109.0, 127.2), turned to 180 degrees
- moved R70 4.93 mm to (158.8, 127.2), turned to 180 degrees
- moved R81 4.64 mm to (213.4, 122.0), turned to -90 degrees
- moved D27 4.60 mm to (196.6, 68.4), turned to 180 degrees
- moved C71 4.36 mm to (213.4, 118.0), turned to 90 degrees
- moved R20 3.54 mm to (65.0, 122.2), turned to -90 degrees
- moved C12 3.09 mm to (65.0, 118.2), turned to 90 degrees
- moved R63 2.99 mm to (210.0, 81.7)
- moved C4 2.89 mm to (107.4, 118.0), turned to 90 degrees
- moved C40 2.88 mm to (157.2, 118.0), turned to 90 degrees
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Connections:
- J23 pad 1: NTC2_B -> EL2
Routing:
- net EL2: track 51.4 -> 179.9 mm, vias 2 -> 6
- net Net-(C99-Pad1): track 0.00 -> 77.2 mm, vias 0 -> 2
- net NTC2_A: track 0.00 -> 56.1 mm, vias 0 -> 2
- net OUT3: track 53.9 -> 87.3 mm
- net OUT1: track 52.8 -> 85.8 mm
- net OUT2: track 53.9 -> 86.0 mm
- net RST_H2: track 0.00 -> 22.0 mm
- net +5VD: track 108.3 -> 122.3 mm, vias 33 -> 35
- net +15V_L2: track 15.0 -> 28.2 mm, vias 14 -> 15
- net Net-(D27-Pad2): track 17.1 -> 27.2 mm
- net Net-(C97-Pad1): track 0.00 -> 9.79 mm, vias 0 -> 1
- net Net-(D40-Pad2): track 0.25 -> 7.88 mm
- net Net-(D35-Pad2): track 0.01 -> 7.62 mm
- net Net-(D12-Pad2): track 0.00 -> 7.35 mm
- net FLT_H2: track 28.3 -> 34.1 mm
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- removed copper zone on B.Cu, net OUT1
- removed copper zone on B.Cu, net OUT2
- removed copper zone on B.Cu, net OUT3
